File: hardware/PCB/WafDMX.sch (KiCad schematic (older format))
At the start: 63 parts, among them J1 Wuerth_7499010121A, J2 Screw_Terminal_01x02, J3 USB_B_Micro, J4 Conn_01x04_Female, J5 XLR3, J6 XLR3, P1 POW_OUT, P2 POW_OUT, P3 POW_OUT, P4 POW_OUT, Q1 MMDT2222A, U1 AMS1117-3.3, U2 LAN8720A, U3 CH340C, U4 ESP32-WROOM-32D, U5 MAX3485, U6 TXB0102DCU, X1 ASV-50MHz

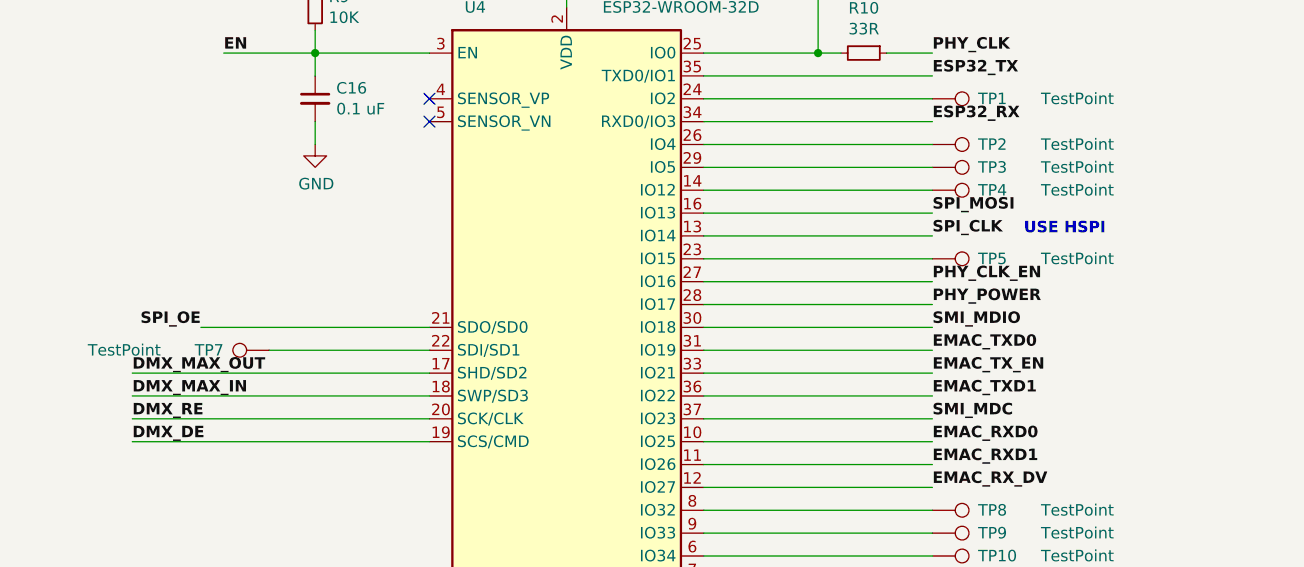
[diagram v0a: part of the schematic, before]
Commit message: Mode SPI_OE on GPIO13
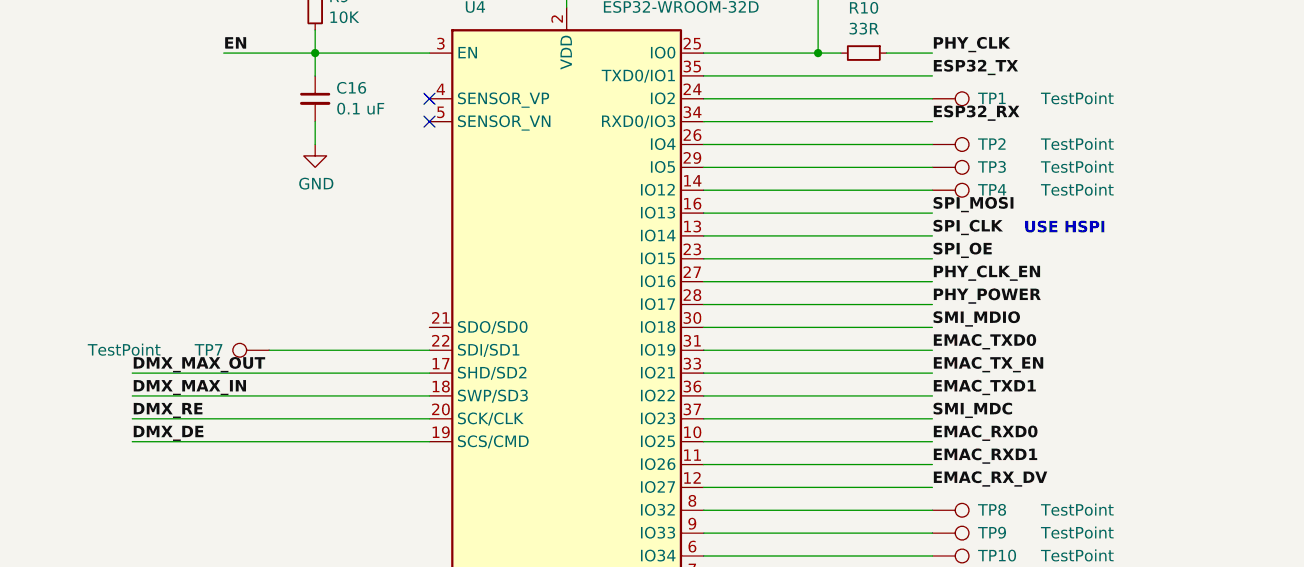
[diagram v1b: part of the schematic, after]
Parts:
- removed TP5: TestPoint, TestPoint:TestPoint_THTPad_1.0x1.0mm_Drill0.5mm, symbol WafDMX-rescue:TestPoint-Connector-WafDMX-rescue
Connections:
- net SPI_OE: now also U4.23 (IO15); no longer U4.21 (SDO/SD0)
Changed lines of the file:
@@
 Wire Wire Line
 	3500 7500 4500 7500
-$Comp
-L WafDMX-rescue:TestPoint-Connector-WafDMX-rescue TP5
-U 1 1 5D2216FB
-P 4500 7800
-F 0 "TP5" V 4500 8000 50  0000 L CNN
-F 1 "TestPoint" V 4500 8275 50  0000 L CNN
-F 2 "TestPoint:TestPoint_THTPad_1.0x1.0mm_Drill0.5mm" H 4700 7800 50  0001 C CNN
-F 3 "~" H 4700 7800 50  0001 C CNN
-F 4 "-" H 0   0   50  0001 C CNN "Part Number"
-	1    4500 7800
-	0    1    1    0
-$EndComp
 Wire Wire Line
 	3500 7800 4500 7800
@@
 Wire Wire Line
 	6600 4500 6600 4600
-Text Label 1300 8100 2    50   ~ 10
+Text Label 4500 7800 0    50   ~ 10
 SPI_OE
-Wire Wire Line
-	2300 8100 1300 8100
 $Comp
 L Device:R_Small R13

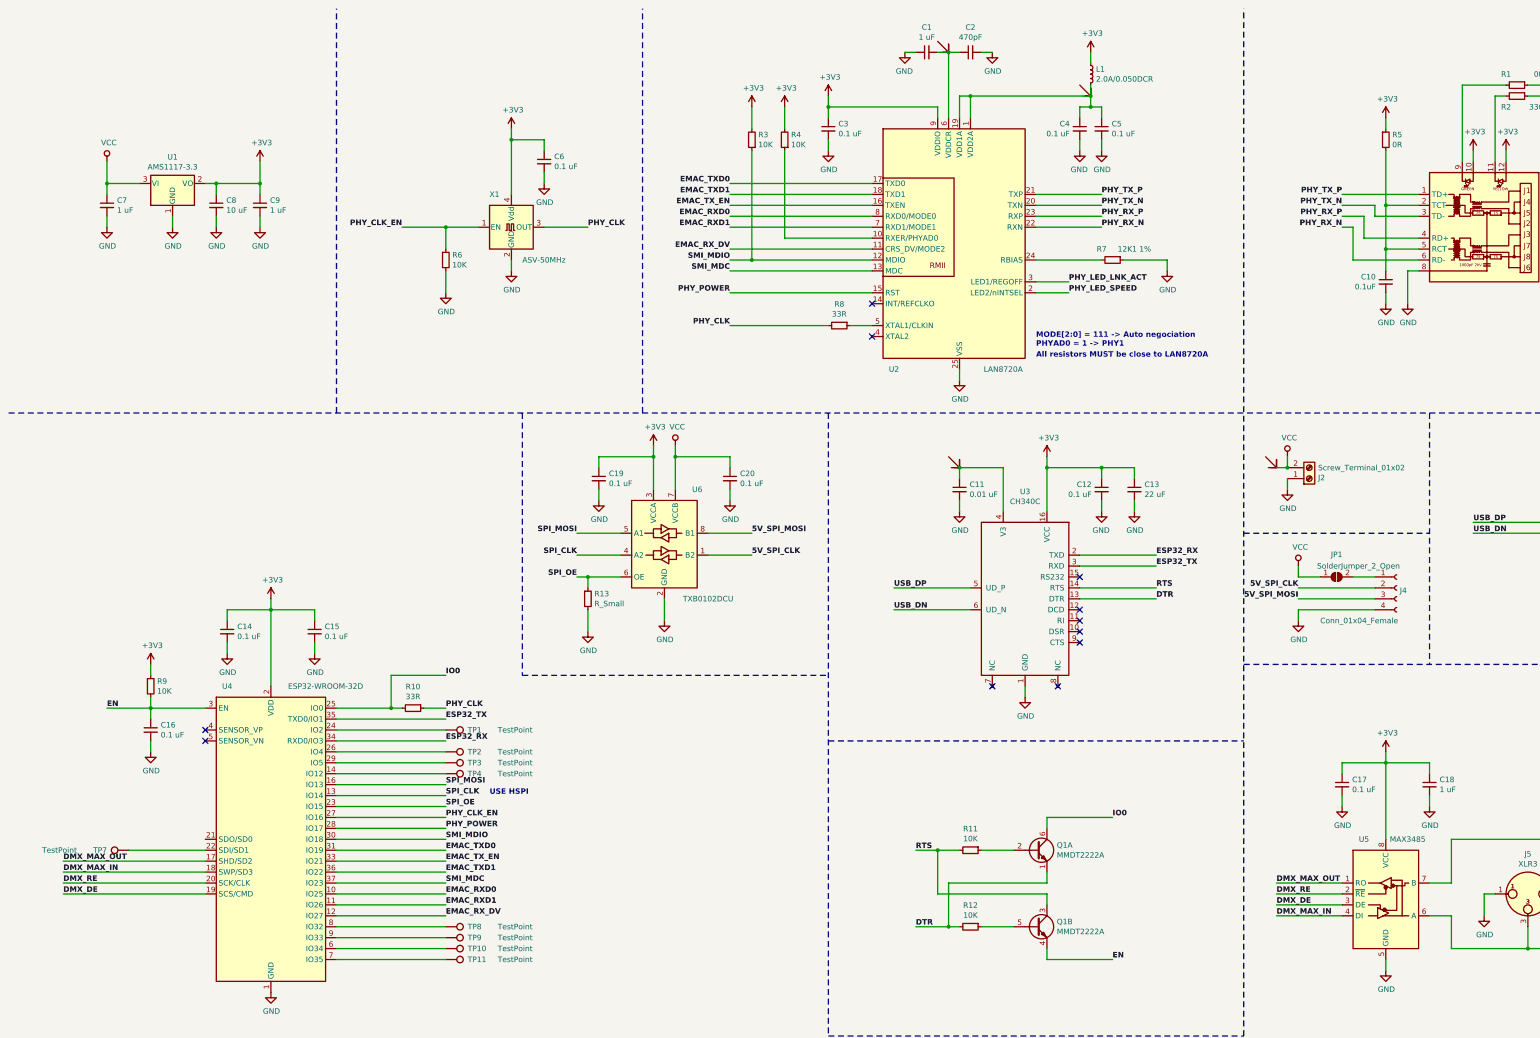
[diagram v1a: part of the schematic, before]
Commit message: Uniformise component values
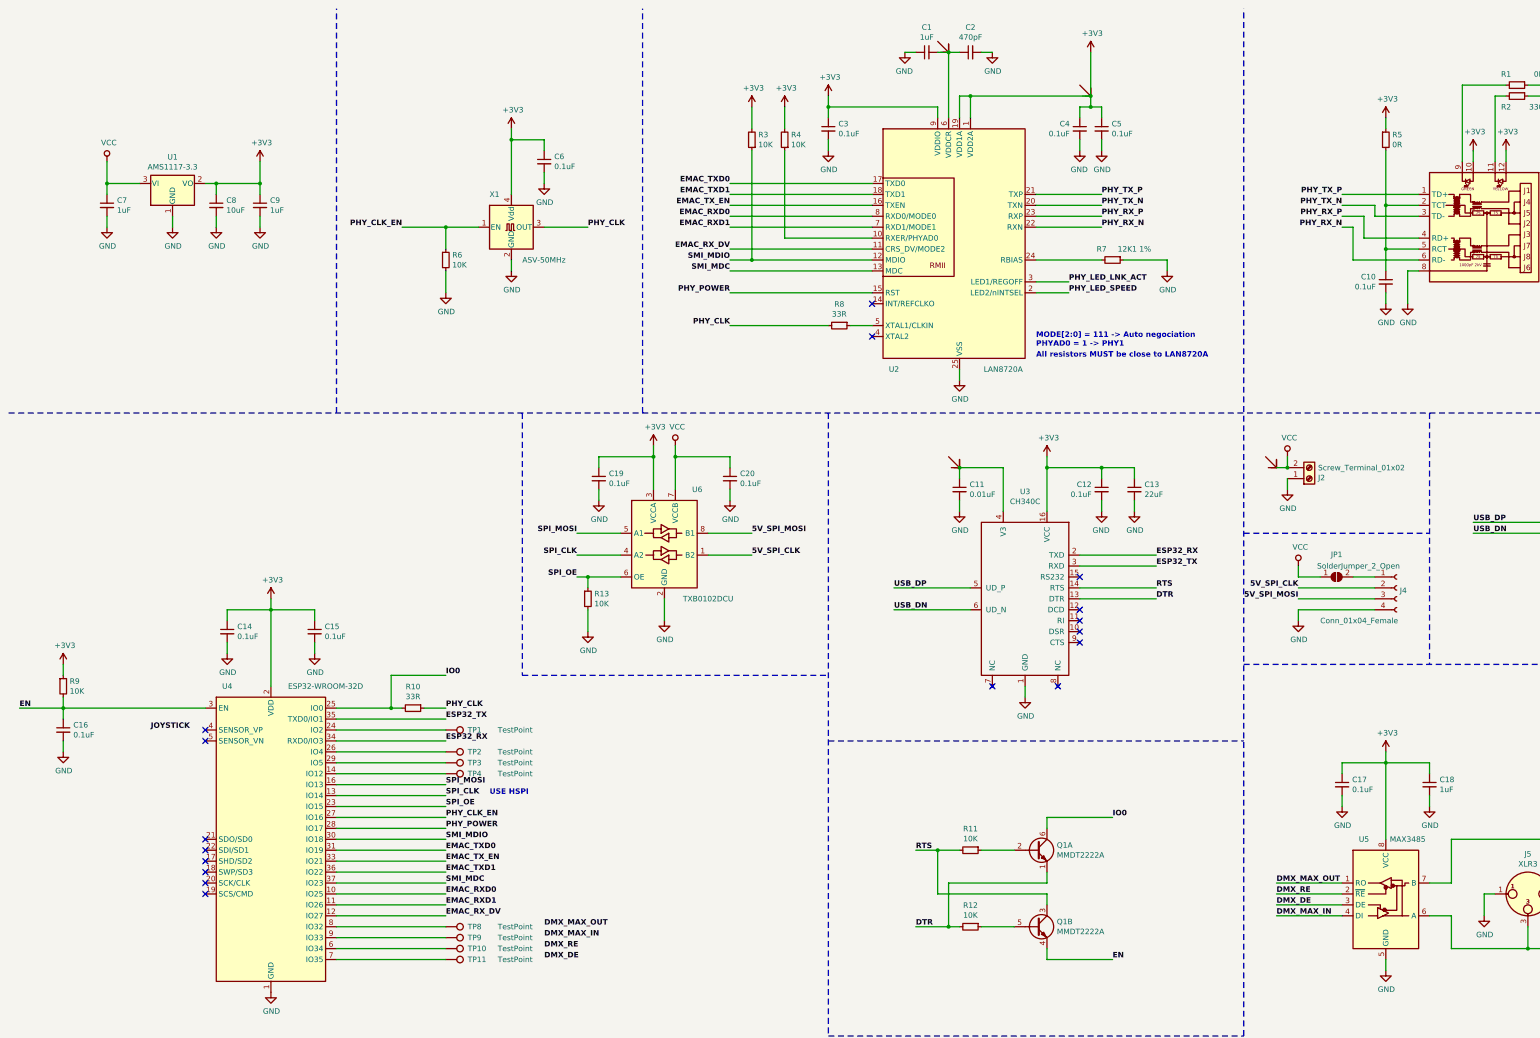
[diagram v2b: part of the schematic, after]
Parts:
- removed L1: 2.0A/0.050DCR, Inductor_SMD:L_0603_1608Metric, symbol WafDMX-rescue:L_Small-Device-WafDMX-rescue
- removed TP7: TestPoint, TestPoint:TestPoint_THTPad_1.0x1.0mm_Drill0.5mm, symbol WafDMX-rescue:TestPoint-Connector-WafDMX-rescue
- C1, C18, C7, C9: value 1 uF -> 1uF
- C11: value 0.01 uF -> 0.01uF
- C12, C14, C15, C16, C17, C19, C20, C3, C4, C5, C6: value 0.1 uF -> 0.1uF
- C13: value 22 uF -> 22uF
- C8: value 10 uF -> 10uF
- R13: value R_Small -> 10K
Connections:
- net +3V3: now also C4.1, C5.1, P4.~, U2.1 (VDD2A), U2.19 (VDD1A)
- net DMX_DE: no longer U4.19 (SCS/CMD)
- net DMX_MAX_IN: no longer U4.18 (SWP/SD3)
- net DMX_MAX_OUT: no longer U4.17 (SHD/SD2)
- net DMX_RE: no longer U4.20 (SCK/CLK)
- no-connect marks 13 -> 19
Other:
- moved on the sheet: C16, R9

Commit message: Add FPGA and LCD screen, bump to v2
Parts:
- removed C19, C20: 0.1uF, Capacitor_SMD:C_0603_1608Metric, symbol WafDMX-rescue:C_Small-Device-WafDMX-rescue
- removed J2: Screw_Terminal_01x02, WafDMX:TerminalBlock_WAGO_2604-1102_2x05_P5.00mm_30Degree, symbol WafDMX-rescue:Screw_Terminal_01x02-Connector-WafDMX-rescue
- removed P4: POW_OUT, symbol WafDMX:POW_OUT
- removed TP1, TP10, TP11, TP2, TP3, TP4, TP8, TP9: TestPoint, TestPoint:TestPoint_THTPad_1.0x1.0mm_Drill0.5mm, symbol WafDMX-rescue:TestPoint-Connector-WafDMX-rescue
- removed U6: TXB0102DCU, Package_SO:VSSOP-8_2.4x2.1mm_P0.5mm, symbol Logic_LevelTranslator:TXB0102DCU
- added C14, C24, C25, C26, C27, C28, C29, C30, C31, C32, C33, C34, C35, C37, C38, C39, C40, C41, C42, C43, C44, C45, C46, C47, C48, C49, C50: 0.1uF, Capacitor_SMD:C_0402_1005Metric, symbol WafDMX-rescue:C_Small-Device-WafDMX-rescue
- added C36, C6, C7, C8, C9: 1uF, Capacitor_SMD:C_0402_1005Metric, symbol WafDMX-rescue:C_Small-Device-WafDMX-rescue
- added J1, J2: Barrel_Jack_Switch, Connector_BarrelJack:BarrelJack_Horizontal, symbol Connector:Barrel_Jack_Switch
- added J10, J11, J12, J13, J14, J15, J16, J17, J18, J19, J20, J21, J22, J23, J24, J25, J26, J8, J9: Conn_01x04_Female, Connector_PinHeader_2.54mm:PinHeader_1x04_P2.54mm_Vertical, symbol WafDMX-rescue:Conn_01x04_Female-Connector-WafDMX-rescue
- added JP2, JP3: SolderJumper_2_Open, Jumper:SolderJumper-2_P1.3mm_Open_Pad1.0x1.5mm, symbol WafDMX-rescue:SolderJumper_2_Open-Jumper-WafDMX-rescue
- added P3: POW_OUT, symbol WafDMX:POW_OUT
- added R15, R16, R7: 10K, Resistor_SMD:R_0402_1005Metric, symbol WafDMX-rescue:R_Small-Device-WafDMX-rescue
- added TP1, TP2, TP3, TP4, TP5, TP6, TP7, TP8: TestPoint, TestPoint:TestPoint_Plated_Hole_D2.0mm, symbol Connector:TestPoint
- added U10, U11, U12, U13, U9: TXB0108, Package_SO:TSSOP-20_4.4x6.5mm_P0.65mm, symbol WafDMX:TXB0108
- added U14: ICE40HX1K-VQ100, WafDMX:VQFP100_Pitch-0.5mm_Dimensions-16.00x16.00x1.20mm, symbol WafDMX:ICE40HX1K-VQ100
- added U2: LN1134A252MR-G, Package_TO_SOT_SMD:SOT-23-5, symbol Regulator_Linear:AP2127K-2.5
- added U3: SGM2019-ADJYN5G/TR, Package_TO_SOT_SMD:SOT-23-5, symbol Regulator_Linear:AP2127K-1.2
- added U8: TFT_LCD_ILI9341, WafDMX:LCD_TFT_ILI9341, symbol WafDMX:TFT_LCD_ILI9341
- added X1: O7050100MEDH4MI, Crystal:Crystal_SMD_FOX_FQ7050-4Pin_7.0x5.0mm, symbol Oscillator:ASE-xxxMHz
- C1: footprint Capacitor_SMD:C_0603_1608Metric -> Capacitor_SMD:C_0402_1005Metric; Part Number 2470425 -> C408910
- C10: renamed from C3; footprint Capacitor_SMD:C_0603_1608Metric -> Capacitor_SMD:C_0402_1005Metric; Part Number 2688469 -> C41851
- C11: renamed from C4; footprint Capacitor_SMD:C_0603_1608Metric -> Capacitor_SMD:C_0402_1005Metric; Part Number 2688469 -> C41851
- C12: renamed from C5; footprint Capacitor_SMD:C_0603_1608Metric -> Capacitor_SMD:C_0402_1005Metric; Part Number 2688469 -> C41851
- C13: renamed from C10; footprint Capacitor_SMD:C_0603_1608Metric -> Capacitor_SMD:C_0402_1005Metric; Part Number 2688469 -> C41851
- C15: renamed from C6; footprint Capacitor_SMD:C_0603_1608Metric -> Capacitor_SMD:C_0402_1005Metric; Part Number 2688469 -> C41851
- C16: renamed from C17; footprint Capacitor_SMD:C_0603_1608Metric -> Capacitor_SMD:C_0402_1005Metric; Part Number 2688469 -> C41851
- C17: renamed from C18; footprint Capacitor_SMD:C_0603_1608Metric -> Capacitor_SMD:C_0402_1005Metric; Part Number 2470425 -> C408910
- C18: renamed from C14; footprint Capacitor_SMD:C_0603_1608Metric -> Capacitor_SMD:C_0402_1005Metric; Part Number 2688469 -> C41851
- C19: renamed from C15; footprint Capacitor_SMD:C_0603_1608Metric -> Capacitor_SMD:C_0402_1005Metric; Part Number 2688469 -> C41851
- C2: footprint Capacitor_SMD:C_0603_1608Metric -> Capacitor_SMD:C_0402_1005Metric; Part Number 8819904 -> C301945
- C20: renamed from C16; footprint Capacitor_SMD:C_0603_1608Metric -> Capacitor_SMD:C_0402_1005Metric; Part Number 2688469 -> C41851
- C21: renamed from C11; footprint Capacitor_SMD:C_0603_1608Metric -> Capacitor_SMD:C_0402_1005Metric; Part Number 2470432 -> C267411
- C22: renamed from C12; footprint Capacitor_SMD:C_0603_1608Metric -> Capacitor_SMD:C_0402_1005Metric; Part Number 2688469 -> C41851
- C23: renamed from C13; footprint Capacitor_SMD:C_1206_3216Metric -> Capacitor_SMD:C_0805_2012Metric; Part Number 1735533 -> C296079
- C3: renamed from C7; footprint Capacitor_SMD:C_0603_1608Metric -> Capacitor_SMD:C_0402_1005Metric; Part Number 2470425 -> C408910
- C4: renamed from C8; footprint Capacitor_SMD:C_1206_3216Metric -> Capacitor_SMD:C_0603_1608Metric; Part Number 2672214RL -> C1691
- C5: renamed from C9; footprint Capacitor_SMD:C_0603_1608Metric -> Capacitor_SMD:C_0402_1005Metric; Part Number 2470425 -> C408910
- J3: renamed from J1; value Wuerth_7499010121A -> HR913129A; footprint Connector_RJ:RJ45_Wuerth_7499010121A_Horizontal -> Connector_RJ:RJ45_Hanrun_HR911105A; Part Number 1636379 -> C70302
- J4: renamed from J5; Part Number 724518 -> C368464
- J5: renamed from J6; Part Number 724543 -> C368463
- J6: renamed from J3; Part Number 2293836 -> C283552
- J7: renamed from J4; Part Number - -> C358686
- JP1, P1, P2: Part Number - -> (none)
- P4: renamed from P3; Part Number - -> (none)
- Q1: Part Number 2317636 -> C96379
- R1: footprint Resistor_SMD:R_0603_1608Metric -> Resistor_SMD:R_0402_1005Metric; Part Number 1469739 -> C60485
- R10: renamed from R9; footprint Resistor_SMD:R_0603_1608Metric -> Resistor_SMD:R_0402_1005Metric; Part Number 2303192 -> C384389
- R11: renamed from R10; footprint Resistor_SMD:R_0603_1608Metric -> Resistor_SMD:R_0402_1005Metric; Part Number 9238301 -> C25161
- R12: renamed from R11; footprint Resistor_SMD:R_0603_1608Metric -> Resistor_SMD:R_0402_1005Metric; Part Number 2303192 -> C384389
- R13: renamed from R12; footprint Resistor_SMD:R_0603_1608Metric -> Resistor_SMD:R_0402_1005Metric; Part Number 2303192 -> C384389
- R14: renamed from R13; footprint Resistor_SMD:R_0603_1608Metric -> Resistor_SMD:R_0402_1005Metric; Part Number 2303192 -> C384389
- R2: footprint Resistor_SMD:R_0603_1608Metric -> Resistor_SMD:R_0402_1005Metric; Part Number 1469803 -> C12246
- R3: renamed from R5; footprint Resistor_SMD:R_0603_1608Metric -> Resistor_SMD:R_0402_1005Metric; Part Number 1469739 -> C60485
- R4: renamed from R3; footprint Resistor_SMD:R_0603_1608Metric -> Resistor_SMD:R_0402_1005Metric; Part Number 2303192 -> C384389
- R5: renamed from R4; footprint Resistor_SMD:R_0603_1608Metric -> Resistor_SMD:R_0402_1005Metric; Part Number 2303192 -> C384389
- R6: renamed from R7; footprint Resistor_SMD:R_0603_1608Metric -> Resistor_SMD:R_0402_1005Metric; Part Number 2447244 -> C25852
- R8: footprint Resistor_SMD:R_0603_1608Metric -> Resistor_SMD:R_0402_1005Metric; Part Number 9238301 -> C25161
- R9: renamed from R6; footprint Resistor_SMD:R_0603_1608Metric -> Resistor_SMD:R_0402_1005Metric; Part Number 2303192 -> C384389
- U1: Part Number - -> C6186
- U4: renamed from U2; Part Number 2292578 -> C45223
- U5: value MAX3485 -> TP8485E-SR; Part Number 2512100 -> C94206
- U6: renamed from U4; Part Number - -> C95209
- U7: renamed from U3; Part Number - -> C84681
- X2: renamed from X1; value ASV-50MHz -> S3D50.000000B20F30T; footprint Oscillator:Oscillator_SMD_Abracon_ASV-4Pin_7.0x5.1mm -> Crystal:Crystal_SMD_3225-4Pin_3.2x2.5mm; Part Number 1611840 -> C387445
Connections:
- net +3V3: now also C14.1, C24.1, C25.1, C26.1, C27.1, C28.1, C29.1, C36.1, C37.1, C38.1, C39.1, C40.1, C41.1, C42.1, C43.1, C44.1, C45.1, C46.1, C6.1, C8.1, R15.1, R16.1, R7.2, U10.5 (VCCA), U11.5 (VCCA), U12.5 (VCCA), U13.5 (VCCA), U14.14 (B3_VCCIO), U14.22 (B3_VCCIO), U14.31 (B2_VCCIO), U14.38 (B2_VCCIO), U14.50 (VCC_SPI), U14.58 (B1_VCCIO), U14.6 (B3_VCCIO), U14.67 (B1_VCCIO), U14.88 (B0_VCCIO), U14.92 (B0_VCCIO), U2.1 (VIN), U2.3 (EN), U3.1 (VIN), U3.3 (EN), U8.1 (VCC), U9.5 (VCCA), X1.4 (Vdd)
- net DMX_DE: now also U6.7 (IO35), U14.71 (IOR_69)
- net DMX_MAX_IN: now also U6.9 (IO33), U14.73 (IOR_71)
- net DMX_MAX_OUT: now also U6.8 (IO32), U14.74 (IOR_72)
- net DMX_RE: now also U6.6 (IO34), U14.72 (IOR_70)
- net GND: now also C14.2, C24.2, C25.2, C26.2, C27.2, C28.2, C29.2, C30.2, C31.2, C32.2, C33.2, C34.2, C35.2, C36.2, C37.2, C38.2, C39.2, C40.2, C41.2, C42.2, C43.2, C44.2, C45.2, C46.2, C47.2, C48.2, C49.2, C50.2, C6.2, C7.2, C8.2, C9.2, J1.2, J1.3, J10.4 (Pin_4), J11.4 (Pin_4), J12.4 (Pin_4), J13.4 (Pin_4), J14.4 (Pin_4), J15.4 (Pin_4), J16.4 (Pin_4), J17.4 (Pin_4), J18.4 (Pin_4), J19.4 (Pin_4), J2.2, J2.3, J20.4 (Pin_4), J21.4 (Pin_4), J22.4 (Pin_4), J23.4 (Pin_4), J24.4 (Pin_4), J25.4 (Pin_4), J26.4 (Pin_4), J8.4 (Pin_4), J9.4 (Pin_4), U10.11 (GND), U11.11 (GND), U12.11 (GND), U13.11 (GND), U14.17 (GND), U14.23 (GND), U14.32 (GND), U14.39 (GND), U14.47 (GND), U14.5 (GND), U14.55 (GND), U14.70 (GND), U14.84 (GND), U14.98 (GND), U2.2 (GND), U3.2 (GND), U8.2 (GND), U9.11 (GND), X1.2 (GND)
- net SPI_OE: now also U10.6 (OE), U11.6 (OE), U12.6 (OE), U13.6 (OE), U14.53 (IOR_54), U9.6 (OE); no longer U6.23 (IO15)
- net VCC: now also C30.1, C31.1, C32.1, C33.1, C34.1, C35.1, J1.1, JP3.2 (B), U10.19 (VCCB), U11.19 (VCCB), U12.19 (VCCB), U13.19 (VCCB), U9.19 (VCCB); no longer JP1.1 (A)
- net FPGA_SDO: now reaches U6.14 (IO12)
- net FPGA_SDO: now also JP1.2 (B), U14.45 (IOB_44_SDO)
- net FPGA_QUADWP: now reaches U6.24 (IO2)
- net FPGA_QUADWP: now also U14.52 (IOR_53)
- net FPGA_QUADHD: now reaches U6.26 (IO4)
- net FPGA_QUADHD: now also U14.51 (IOR_52)
- net FPGA_RST: now reaches U6.29 (IO5)
- net FPGA_RST: now also R15.2, U14.44 (CRESET_B)
- net FPGA_RDY: now reaches U6.4 (SENSOR_VP)
- net FPGA_RDY: now also R16.2, U14.43 (CDONE)
- net VDD_LED: now reaches J7.1 (Pin_1)
- net VDD_LED: now also J10.1 (Pin_1), J11.1 (Pin_1), J12.1 (Pin_1), J13.1 (Pin_1), J14.1 (Pin_1), J15.1 (Pin_1), J16.1 (Pin_1), J17.1 (Pin_1), J18.1 (Pin_1), J19.1 (Pin_1), J2.1, J20.1 (Pin_1), J21.1 (Pin_1), J22.1 (Pin_1), J23.1 (Pin_1), J24.1 (Pin_1), J25.1 (Pin_1), J26.1 (Pin_1), J8.1 (Pin_1), J9.1 (Pin_1), JP3.1 (A), P3.~; no longer JP1.2 (B)
- net 5V_SPI_CLK renamed 5V_OUT_0
- net 5V_OUT_0: now also U9.20 (B1)
- net 5V_SPI_MOSI renamed 5V_OUT_1
- net 5V_OUT_1: now also U9.18 (B2)
- net SPI_CLK renamed FPGA_SCK
- net FPGA_SCK: now also JP2.2 (B), U14.48 (IOB_46_SCK)
- net SPI_MOSI renamed FPGA_SDI
- net FPGA_SDI: now also U14.46 (IOB_45_SDI)
- new net: TP8.1, U14.78 (IOT_73)
- new net: TP7.1, U14.79 (IOT_74)
- new net: TP6.1, U14.80 (IOT_75)
- new net: TP5.1, U14.81 (IOT_77)
- new net: TP4.1, U14.82 (IOT_78)
- new net: TP3.1, U14.83 (IOT_79)
- new net: TP2.1, U14.85 (IOT_80)
- new net: TP1.1, U14.86 (IOT_81)
- new net: R7.1, X1.1 (EN)
- new net +1V2: C47.1, C48.1, C49.1, C50.1, C9.1, U14.11 (VCC), U14.35 (VCC), U14.61 (VCC), U14.77 (VCC), U3.5 (VOUT)
- new net +2V5: C7.1, U14.75 (VPP_2V5), U2.5 (VOUT)
- new net 5V_OUT_10: J8.2 (Pin_2), U10.17 (B3)
- new net 5V_OUT_11: J8.3 (Pin_3), U10.16 (B4)
- new net 5V_OUT_12: J12.2 (Pin_2), U10.15 (B5)
- new net 5V_OUT_13: J12.3 (Pin_3), U10.14 (B6)
- new net 5V_OUT_14: J16.2 (Pin_2), U10.13 (B7)
- new net 5V_OUT_15: J16.3 (Pin_3), U10.12 (B8)
- new net 5V_OUT_16: J20.2 (Pin_2), U11.20 (B1)
- new net 5V_OUT_17: J20.3 (Pin_3), U11.18 (B2)
- new net 5V_OUT_18: J24.2 (Pin_2), U11.17 (B3)
- new net 5V_OUT_19: J24.3 (Pin_3), U11.16 (B4)
- new net 5V_OUT_2: J11.2 (Pin_2), U9.17 (B3)
- new net 5V_OUT_20: J9.2 (Pin_2), U11.15 (B5)
- new net 5V_OUT_21: J9.3 (Pin_3), U11.14 (B6)
- new net 5V_OUT_22: J13.2 (Pin_2), U11.13 (B7)
- new net 5V_OUT_23: J13.3 (Pin_3), U11.12 (B8)
- new net 5V_OUT_24: J17.2 (Pin_2), U12.20 (B1)
- new net 5V_OUT_25: J17.3 (Pin_3), U12.18 (B2)
- new net 5V_OUT_26: J21.2 (Pin_2), U12.17 (B3)
- new net 5V_OUT_27: J21.3 (Pin_3), U12.16 (B4)
- new net 5V_OUT_28: J25.2 (Pin_2), U12.15 (B5)
- new net 5V_OUT_29: J25.3 (Pin_3), U12.14 (B6)
- new net 5V_OUT_3: J11.3 (Pin_3), U9.16 (B4)
- new net 5V_OUT_30: J10.2 (Pin_2), U12.13 (B7)
- new net 5V_OUT_31: J10.3 (Pin_3), U12.12 (B8)
- new net 5V_OUT_32: J14.2 (Pin_2), U13.20 (B1)
- new net 5V_OUT_33: J14.3 (Pin_3), U13.18 (B2)
- new net 5V_OUT_34: J18.2 (Pin_2), U13.17 (B3)
- new net 5V_OUT_35: J18.3 (Pin_3), U13.16 (B4)
- new net 5V_OUT_36: J22.2 (Pin_2), U13.15 (B5)
- new net 5V_OUT_37: J22.3 (Pin_3), U13.14 (B6)
- new net 5V_OUT_38: J26.2 (Pin_2), U13.13 (B7)
- new net 5V_OUT_39: J26.3 (Pin_3), U13.12 (B8)
- new net 5V_OUT_4: J15.2 (Pin_2), U9.15 (B5)
- new net 5V_OUT_5: J15.3 (Pin_3), U9.14 (B6)
- new net 5V_OUT_6: J19.2 (Pin_2), U9.13 (B7)
- new net 5V_OUT_7: J19.3 (Pin_3), U9.12 (B8)
- new net 5V_OUT_8: J23.2 (Pin_2), U10.20 (B1)
- new net 5V_OUT_9: J23.3 (Pin_3), U10.18 (B2)
- new net FPGA_SS: U14.49 (IOB_47_SS), U6.23 (IO15)
- new net FPGA_SYSCLK: U14.15 (IOL_7A_GBIN6), X1.3 (OUT)
- new net LCD_CLK: U14.62 (IOR_60_GBIN3), U8.7 (CLK)
- new net LCD_CS: U14.65 (IOR_64), U8.3 (CS)
- new net LCD_DC: U14.68 (IOR_67), U8.5 (DC)
- new net LCD_LED: U14.66 (IOR_65), U8.8 (LED)
- new net LCD_MISO: U14.63 (IOR_61_GBIN2), U8.9 (MISO)
- new net LCD_MOSI: U14.64 (IOR_63), U8.6 (MOSI)
- new net LCD_RST: U14.69 (IOR_68), U8.4 (RST)
- new net LCD_T_CLK: U14.56 (IOR_56), U8.10 (T_CLK)
- new net LCD_T_CS: U14.60 (IOR_59), U8.11 (T_CS)
- new net LCD_T_IRQ: U14.54 (IOR_55), U8.14 (T_IRQ)
- new net LCD_T_MISO: U14.57 (IOR_57), U8.13 (T_MISO)
- new net LCD_T_MOSI: U14.59 (IOR_58), U8.12 (T_MOSI)
- new net OUT_0: JP1.1 (A), U14.1 (IOL_1A), U9.1 (A1)
- new net OUT_1: JP2.1 (A), U14.2 (IOL_1B), U9.2 (A2)
- new net OUT_10: U10.3 (A3), U14.16 (IOL_7B)
- new net OUT_11: U10.4 (A4), U14.18 (IOL_8A)
- new net OUT_12: U10.7 (A5), U14.19 (IOL_8B)
- new net OUT_13: U10.8 (A6), U14.20 (IOL_10A)
- new net OUT_14: U10.9 (A7), U14.21 (IOL_10B)
- new net OUT_15: U10.10 (A8), U14.24 (IOL_12A)
- new net OUT_16: U11.1 (A1), U14.25 (IOL_12B)
- new net OUT_17: U11.2 (A2), U14.26 (IOB_26)
- new net OUT_18: U11.3 (A3), U14.27 (IOB_27)
- new net OUT_19: U11.4 (A4), U14.28 (IOB_28)
- new net OUT_2: U14.3 (IOL_2A), U9.3 (A3)
- new net OUT_20: U11.7 (A5), U14.29 (IOB_29)
- new net OUT_21: U11.8 (A6), U14.30 (IOB_30)
- new net OUT_22: U11.9 (A7), U14.33 (IOB_35_GBIN5)
- new net OUT_23: U11.10 (A8), U14.34 (IOB_36_GBIN4)
- new net OUT_24: U12.1 (A1), U14.36 (IOB_34)
- new net OUT_25: U12.2 (A2), U14.37 (IOB_37)
- new net OUT_26: U12.3 (A3), U14.40 (IOB_41)
- new net OUT_27: U12.4 (A4), U14.41 (IOB_42_CBSEL0)
- new net OUT_28: U12.7 (A5), U14.42 (IOB_43_CBSEL1)
- new net OUT_29: U12.8 (A6), U14.100 (IOT_95)
- new net OUT_3: U14.4 (IOL_2B), U9.4 (A4)
- new net OUT_30: U12.9 (A7), U14.99 (IOT_93)
- new net OUT_31: U12.10 (A8), U14.97 (IOT_91)
- new net OUT_32: U13.1 (A1), U14.96 (IOT_90)
- new net OUT_33: U13.2 (A2), U14.95 (IOT_89)
- new net OUT_34: U13.3 (A3), U14.94 (IOT_88)
- new net OUT_35: U13.4 (A4), U14.93 (IOT_87)
- new net OUT_36: U13.7 (A5), U14.91 (IOT_86)
- new net OUT_37: U13.8 (A6), U14.90 (IOT_85_GBIN0)
- new net OUT_38: U13.9 (A7), U14.89 (IOT_84_GBIN1)
- new net OUT_39: U13.10 (A8), U14.87 (IOT_82)
- new net OUT_4: U14.7 (IOL_3A), U9.7 (A5)
- new net OUT_5: U14.8 (IOL_3B), U9.8 (A6)
- new net OUT_6: U14.9 (IOL_5A), U9.9 (A7)
- new net OUT_7: U14.10 (IOL_5B), U9.10 (A8)
- new net OUT_8: U10.1 (A1), U14.12 (IOL_6A)
- new net OUT_9: U10.2 (A2), U14.13 (IOL_6B_GBIN7)
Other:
- note added: "- Only one output\n- No LCD touch screen\n"
- note added: "100MHz ±20ppm"
- note added: "AHHHH"
- note added: "Isolation selector:\nBy default, the circuitry is powered by VCC, using a different PSU\nthan the LEDs. The circuit can work using the LED PSU by soldering\nthis jumper.\n"
- note added: "USE AT YOUR OWN RISK. DO NOT PLUG THE TWO PSU, OR THEY MAY BE DAMAGED/BURN"
- note added: "Variant selector: \nThe ESP32 can work without the FPGA by soldering these jumpers.\nReduced features:"
- moved on the sheet: C1, C10, C11, C12, C13, C15, C16, C17, C18, C19, C2, C20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
